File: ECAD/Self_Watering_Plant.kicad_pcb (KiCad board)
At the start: 2 copper layers, 50 parts, among them J1 Conn_01x02, J2 Conn_01x02, J3 Conn_01x02, J4 Conn_01x02, J5 Conn_01x02, J6 USB_A, J7 Conn_01x02, J8 Conn_01x02, P1 U262-161N-4BVC11, Q1 BC817, Q2 BC817, Q3 NCE3018AS, Q4 NCE3018AS, Q5 NCE3018AS, Q6 NCE3018AS, Q7 NCE3018AS, Q8 NCE3018AS, SW1 SW_Push, U1 LM393, U10 DHT11, U2 LM393, U3 CH340C, U4 ESP32-WROOM-32, U5 NC7SB3157P6X, U6 NC7SB3157P6X, U7 NC7SB3157P6X

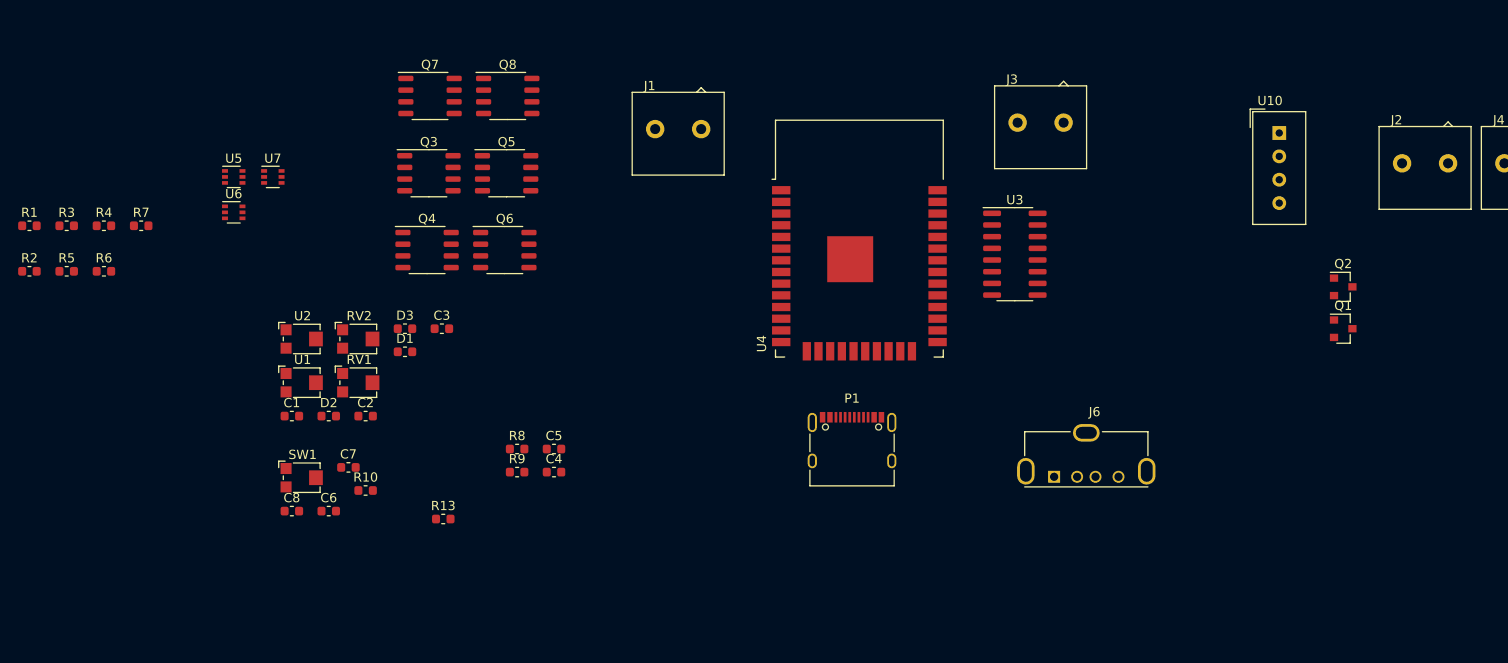
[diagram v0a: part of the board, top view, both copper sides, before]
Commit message: porting project to kicad 5.99, fixing some error in schematics. Getting ready to lay down the layout and order in jlcpcb
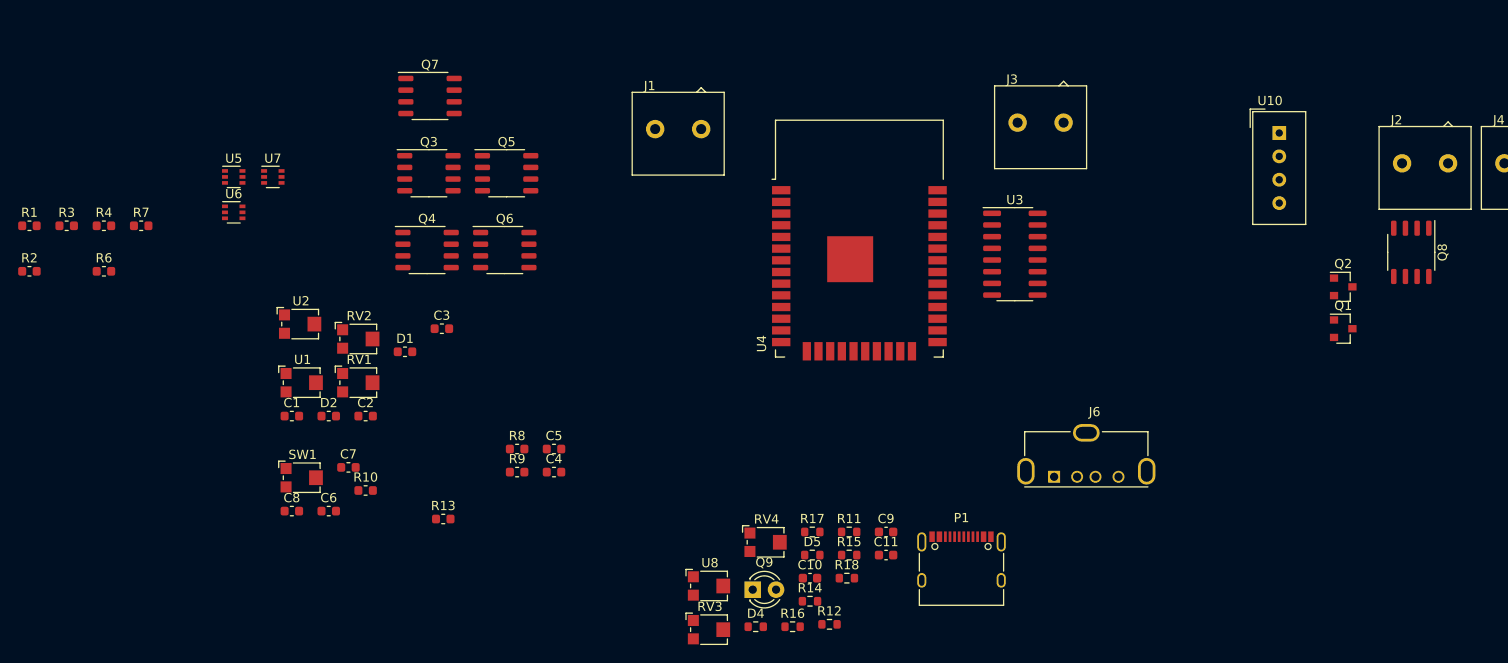
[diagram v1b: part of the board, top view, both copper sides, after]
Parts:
- removed D3: LED, Resistor_SMD:R_0603_1608Metric
- removed R5: 1K, Resistor_SMD:R_0603_1608Metric
- added C10: 10nF, Capacitor_SMD:C_0603_1608Metric, F.Cu at (138.5, 131.3)
- added C11: 10nF, Capacitor_SMD:C_0603_1608Metric, F.Cu at (146.8, 128.8)
- added C9: 100nF, Capacitor_SMD:C_0603_1608Metric, F.Cu at (146.8, 126.3)
- added D4: LED, Resistor_SMD:R_0603_1608Metric, F.Cu at (132.6, 136.6)
- added D5: LED, Resistor_SMD:R_0603_1608Metric, F.Cu at (138.8, 128.8)
- added Q9: TEPT4400, LED_THT:LED_D3.0mm_Clear, F.Cu at (132.3, 132.6)
- added R11: 10K, Resistor_SMD:R_0603_1608Metric, F.Cu at (142.8, 126.3)
- added R12: 10K, Resistor_SMD:R_0603_1608Metric, F.Cu at (140.7, 136.3)
- added R14: 10K, Resistor_SMD:R_0603_1608Metric, F.Cu at (138.5, 133.8)
- added R15: 10K, Resistor_SMD:R_0603_1608Metric, F.Cu at (142.8, 128.8)
- added R16: 10K, Resistor_SMD:R_0603_1608Metric, F.Cu at (136.6, 136.6)
- added R17: 1K, Resistor_SMD:R_0603_1608Metric, F.Cu at (138.8, 126.3)
- added R18: 1K, Resistor_SMD:R_0603_1608Metric, F.Cu at (142.5, 131.3)
- added RV3: 10K, Potentiometer_SMD:Potentiometer_Bourns_TC33X_Vertical, F.Cu at (127.7, 136.9)
- added RV4: 10K, Potentiometer_SMD:Potentiometer_Bourns_TC33X_Vertical, F.Cu at (133.8, 127.4)
- added U8: LM393, Potentiometer_SMD:Potentiometer_Bourns_TC33X_Vertical, F.Cu at (127.7, 132.2)
- moved Q8 99.7 mm to (203.9, 95.9), turned to -90 degrees
- moved P1 17.6 mm to (155.0, 130.5)
- moved U2 1.63 mm to (83.2, 103.7)
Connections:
- net /Controller/AIN renamed /AnalogMux/AOUT
- C4 pad 1: /FlasherCircuit/+5V -> +5V
- J6 pad 1: (no net) -> +5V
- J6 pad 2: (no net) -> unconnected-(J6-Pad2)
- J6 pad 3: (no net) -> unconnected-(J6-Pad3)
- P1 pad A1: Net-(P1-PadA1) -> GND
- P1 pad A12: Net-(P1-PadA1) -> GND
- P1 pad A4: /FlasherCircuit/+5V -> +5V
- P1 pad A5: (no net) -> unconnected-(P1-PadA5)
- P1 pad A9: /FlasherCircuit/+5V -> +5V
- P1 pad B1: Net-(P1-PadA1) -> GND
- P1 pad B12: Net-(P1-PadA1) -> GND
- P1 pad B4: /FlasherCircuit/+5V -> +5V
- P1 pad B5: (no net) -> unconnected-(P1-PadB5)
- P1 pad B9: /FlasherCircuit/+5V -> +5V
- P1 pad S1: Net-(P1-PadS1) -> GND
- Q3 pad 2: (no net) -> /Controller/CTRL_LEDSTRIP_A
- Q4 pad 2: (no net) -> /Controller/CTRL_LEDSTRIP_B
- Q5 pad 2: (no net) -> /Controller/CTRL_LEDSTRIP_C
- Q6 pad 2: (no net) -> /Controller/CTRL_LEDSTRIP_USB
- Q7 pad 2: (no net) -> /Controller/CTRL_WATERPUMP_A
- Q8 pad 2: (no net) -> /Controller/CTRL_WATERPUMP_B
- R13 pad 1: /TempAndHumiditySensor/+3.3V -> +3V3
- R13 pad 2: /TempAndHumiditySensor/IO -> /Controller/DH11_IO
- U10 pad 1: /TempAndHumiditySensor/+3.3V -> +3V3
- U10 pad 2: /TempAndHumiditySensor/IO -> /Controller/DH11_IO
- U10 pad 3: (no net) -> unconnected-(U10-Pad3)
- U2 pad 1: /ALERT1_IS_DRY -> (no net)
- U2 pad 2: Net-(RV2-Pad2) -> (no net)
- U2 pad 3: +3V3 -> (no net)
- U3 pad 10: (no net) -> unconnected-(U3-Pad10)
- U3 pad 11: (no net) -> unconnected-(U3-Pad11)
- U3 pad 12: (no net) -> unconnected-(U3-Pad12)
- U3 pad 15: (no net) -> unconnected-(U3-Pad15)
- U3 pad 16: /FlasherCircuit/+5V -> +5V
- U3 pad 7: (no net) -> unconnected-(U3-Pad7)
- U3 pad 8: (no net) -> unconnected-(U3-Pad8)
- U3 pad 9: (no net) -> unconnected-(U3-Pad9)
- U4 pad 10: (no net) -> unconnected-(U4-Pad10)
- U4 pad 11: (no net) -> unconnected-(U4-Pad11)
- U4 pad 12: (no net) -> unconnected-(U4-Pad12)
- U4 pad 13: (no net) -> /Controller/CTRL_LEDSTRIP_A
- U4 pad 14: (no net) -> /SEL0
- U4 pad 16: (no net) -> /SEL1
- U4 pad 17: (no net) -> unconnected-(U4-Pad17)
- U4 pad 18: (no net) -> unconnected-(U4-Pad18)
- U4 pad 19: (no net) -> unconnected-(U4-Pad19)
- U4 pad 20: (no net) -> unconnected-(U4-Pad20)
- U4 pad 21: (no net) -> unconnected-(U4-Pad21)
- U4 pad 22: (no net) -> unconnected-(U4-Pad22)
- U4 pad 23: (no net) -> /Controller/CTRL_LEDSTRIP_B
- U4 pad 24: (no net) -> unconnected-(U4-Pad24)
- U4 pad 26: (no net) -> /Controller/CTRL_WATERPUMP_A
- U4 pad 27: (no net) -> /Controller/CTRL_LEDSTRIP_C
- U4 pad 28: (no net) -> /Controller/CTRL_LEDSTRIP_USB
- U4 pad 29: (no net) -> /Controller/CTRL_WATERPUMP_B
- U4 pad 30: (no net) -> /ALERT0_IS_DRY
- U4 pad 31: (no net) -> /ALERT1_IS_DRY
- U4 pad 32: (no net) -> unconnected-(U4-Pad32)
- U4 pad 33: (no net) -> /ALERT2_IS_DARK
- U4 pad 36: (no net) -> /ALERT3_CUSTOM
- U4 pad 37: (no net) -> /Controller/DH11_IO
- U4 pad 6: (no net) -> unconnected-(U4-Pad6)
- U4 pad 7: (no net) -> unconnected-(U4-Pad7)
- U4 pad 8: (no net) -> unconnected-(U4-Pad8)
- U4 pad 9: (no net) -> unconnected-(U4-Pad9)
- U5 pad 1: (no net) -> unconnected-(U5-Pad1)
- U5 pad 3: (no net) -> unconnected-(U5-Pad3)
- U5 pad 4: (no net) -> unconnected-(U5-Pad4)
- U5 pad 5: (no net) -> +3V3
- U5 pad 6: (no net) -> unconnected-(U5-Pad6)
- U6 pad 1: (no net) -> unconnected-(U6-Pad1)
- U6 pad 2: (no net) -> unconnected-(U6-Pad2)
- U6 pad 3: (no net) -> unconnected-(U6-Pad3)
- U6 pad 4: (no net) -> unconnected-(U6-Pad4)
- U6 pad 5: (no net) -> unconnected-(U6-Pad5)
- U6 pad 6: (no net) -> unconnected-(U6-Pad6)
- U7 pad 1: (no net) -> unconnected-(U7-Pad1)
- U7 pad 2: (no net) -> unconnected-(U7-Pad2)
- U7 pad 3: (no net) -> unconnected-(U7-Pad3)
- U7 pad 5: (no net) -> unconnected-(U7-Pad5)
- U7 pad 6: (no net) -> /SEL1
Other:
- net class Default removed

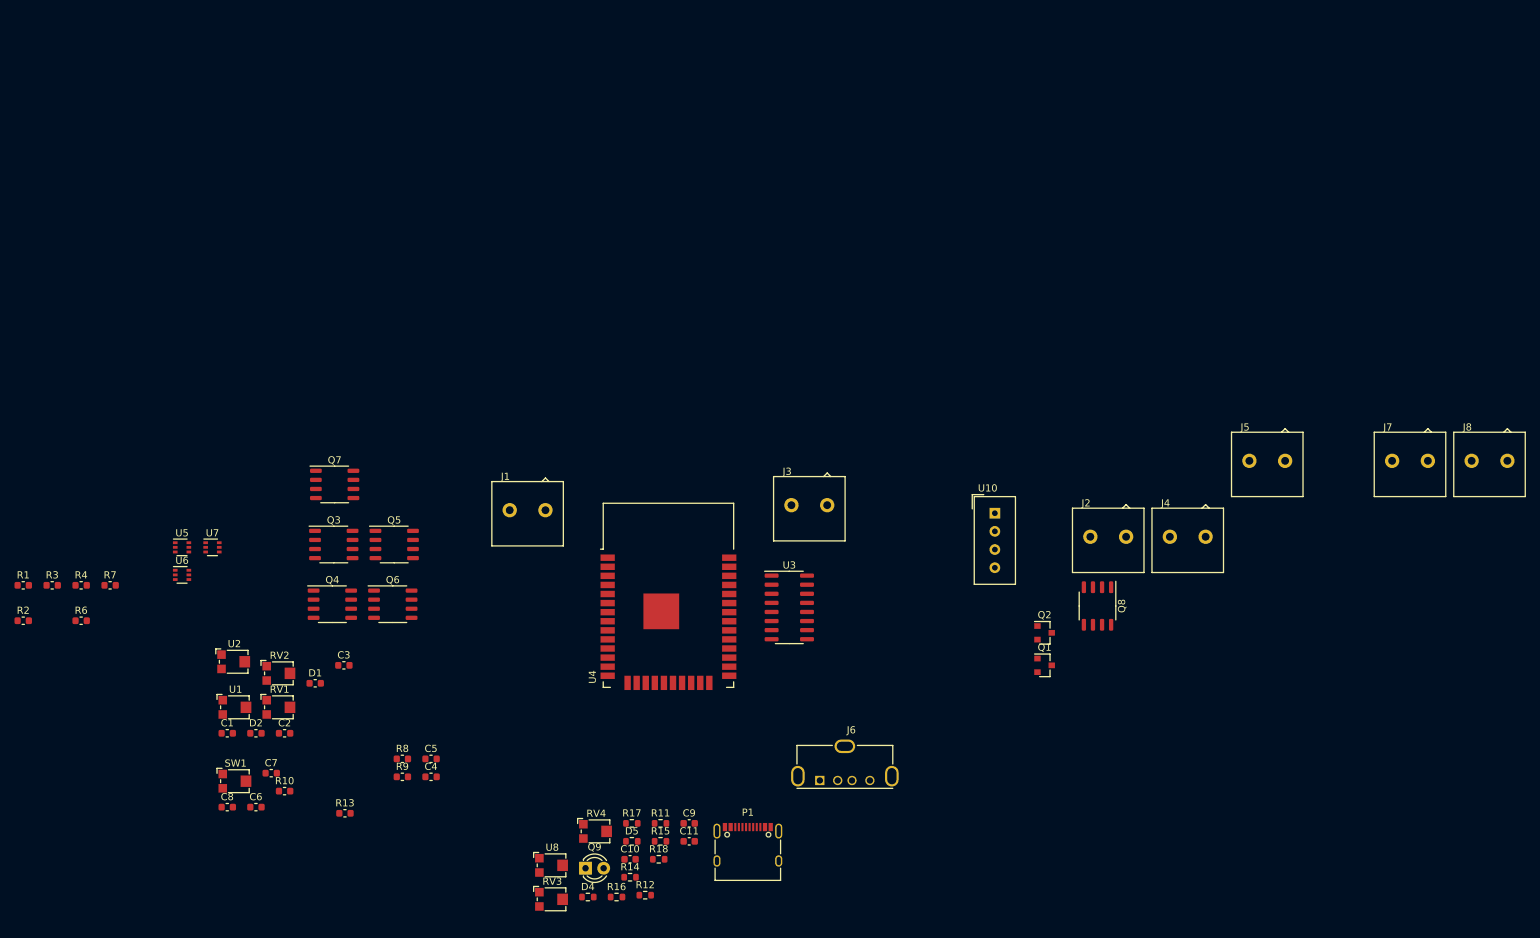
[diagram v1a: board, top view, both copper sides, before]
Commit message: pcb layout has started, still ned to make 5V to 3.3V power supply, add dip switch do individually control input power of each switch, 5V or 12V
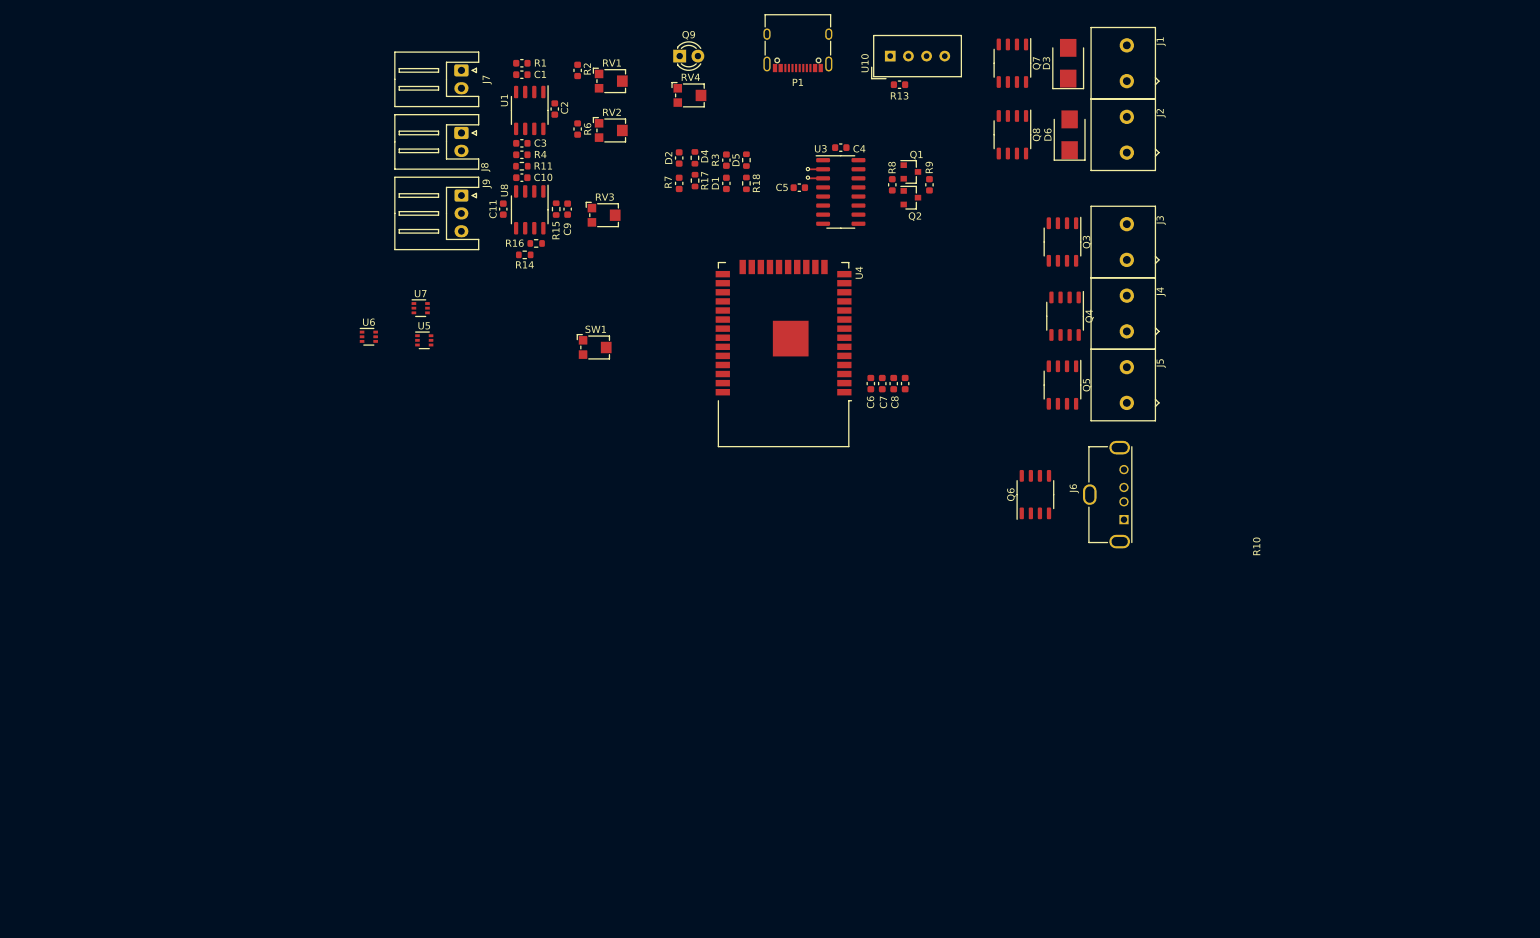
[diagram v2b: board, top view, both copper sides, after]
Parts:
- removed R12: 10K, Resistor_SMD:R_0603_1608Metric
- removed U2: LM393, Potentiometer_SMD:Potentiometer_Bourns_TC33X_Vertical
- added D3: RS3ABG, Diode_SMD:D_SMB, F.Cu at (199.8, 20.0)
- added D6: RS3ABG, Diode_SMD:D_SMB, F.Cu at (200.0, 30.0)
- added J9: Conn_01x03, Connector_JST:JST_XH_S3B-XH-A_1x03_P2.50mm_Horizontal, F.Cu at (115.0, 38.5)
- J7, J8: footprint ConnectorsSMD:TB001-500-02BE -> Connector_JST:JST_XH_S2B-XH-A_1x02_P2.50mm_Horizontal
- U1, U8: value LM393 -> LM293; footprint Potentiometer_SMD:Potentiometer_Bourns_TC33X_Vertical -> Package_SO:SO-8_3.9x4.9mm_P1.27mm
- moved J8 150.9 mm to (115.0, 29.8), turned to -90 degrees
- moved J7 143.4 mm to (115.0, 21.0), turned to -90 degrees
- moved R13 128.0 mm to (176.2, 23.0)
- moved Q9 114.3 mm to (145.5, 19.0)
- moved P1 113.7 mm to (162.0, 17.0), turned to 180 degrees
- moved Q7 111.6 mm to (192.0, 20.0), turned to -90 degrees
- moved R3 111.5 mm to (152.0, 33.5), turned to 90 degrees
- moved R9 110.8 mm to (180.4, 37.0), turned to -90 degrees
- moved C8 110.4 mm to (175.4, 64.8), turned to -90 degrees
- moved Q3 110.3 mm to (199.0, 45.0), turned to -90 degrees
- moved Q4 110.1 mm to (199.4, 55.4), turned to -90 degrees
- moved R2 109.2 mm to (131.2, 21.0), turned to -90 degrees
- moved R8 105.5 mm to (175.2, 37.0), turned to 90 degrees
- moved C4 105.0 mm to (168.0, 31.8), turned to 180 degrees
- moved J1 104.5 mm to (208.0, 20.0), turned to -90 degrees
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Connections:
- C1 pad 1: +3V3 -> /AnalogMux/AIN_0
- C10 pad 1: +3V3 -> /AnalogMux/AIN_2
- C11 pad 1: +3V3 -> /AnalogMux/AIN_3
- C3 pad 1: +3V3 -> /AnalogMux/AIN_1
- J2 pad 2: /WaterPumpControl/WATERPUM_B- -> /WATERPUM_B-
- J7 pad 1: +3V3 -> /AnalogMux/AIN_0
- J8 pad 1: +3V3 -> /AnalogMux/AIN_1
- Q8 pad 1: /WaterPumpControl/WATERPUM_B- -> /WaterPumpControl/WATERPUMP_B-
- Q9 pad 2: +3V3 -> /AnalogMux/AIN_2
- R1 pad 2: +3V3 -> /AnalogMux/AIN_0
- R11 pad 1: +3V3 -> /AnalogMux/AIN_2
- R14 pad 2: +3V3 -> /AnalogMux/AIN_3
- R4 pad 2: +3V3 -> /AnalogMux/AIN_1
- U1 pad 3: +3V3 -> /AnalogMux/AIN_0
- U7 pad 2: unconnected-(U7-Pad2) -> /SEL0
- U8 pad 3: +3V3 -> /AnalogMux/AIN_2
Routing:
- net /Controller/RX: track 0.00 -> 2.16 mm, vias 0 -> 1
- net /Controller/TX: track 0.00 -> 2.14 mm, vias 0 -> 1
